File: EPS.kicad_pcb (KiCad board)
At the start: 4 copper layers, 90.2 x 95.9 mm, 197 parts, among them IC1 BQ7791514PWR, IC10 INA260AIPWR, IC12 LM74700QDBVRQ1, IC13 LM74700QDBVRQ1, IC14 LM5176PWPR, IC15 SN65HVD1782QDRQ1, IC16 TPS2121RUXR, IC17 TCAN1046AVDRQ1, IC18 INA260AIPWR, IC19 LM5060Q1MM_NOPB, IC2 INA260AIPWR, IC20 LM5060Q1MM_NOPB, IC21 MCP2517FD-H_SL, IC3 INA260AIPWR, IC4 INA260AIPWR, IC5 TPS22990DMLR, IC6 TPS22990DMLR, IC7 TPS22990DMLR, IC9 INA260AIPWR, J1 Barrel_Jack_Switch, J2 PH1RA-02-UA, J3 WJ126V-5.0-2P, J4 USB_C_Receptacle_USB2.0_16P, J6 TagConnect_TC2030-NL, Q10 BSZ067N06LS3_G, Q11 BSZ067N06LS3_G, Q12 BSZ067N06LS3_G, Q13 BSZ067N06LS3_G, Q15 BSZ067N06LS3_G, Q16 BSZ067N06LS3_G, Q5 BSZ067N06LS3_G, Q6 BSZ067N06LS3_G, Q8 BSZ067N06LS3_G, Q9 BSZ067N06LS3_G, U2 RP2354A_60QFN, Y1 ABM8AIG-20MHz-12-2Z-T3, Y2 ABM8-272-T3

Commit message: Rev 1 version
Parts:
- removed C36, C41, C43, C44, C46, C47, C50, C54, C57, C58, C59, C60, C61, C62, C63, C64, C66, C67, C75, C89, C90, C91, C92: 100n, Capacitor_SMD:C_0402_1005Metric
- removed C37, C42, C45, C48: 22u, Capacitor_SMD:C_0603_1608Metric
- removed C40: 22n, Capacitor_SMD:C_0402_1005Metric
- removed C49, C51, C55, C73, C74: 1u, Capacitor_SMD:C_0603_1608Metric
- removed C52, C53, C56: 220p, Capacitor_SMD:C_0402_1005Metric
- removed C65, C70, C71, C72: 4u7, Capacitor_SMD:C_0603_1608Metric
- removed C68, C69, C93, C94: 15p, Capacitor_SMD:C_0402_1005Metric
- removed D10, D11, D12, D13: SMCJ36A, HEDGE2:SMCJ36A
- removed D14, D5, D6, D7: CDBA240LL-HF, 40V 2A, HEDGE2:CDBA240LL-HF
- removed IC13: LM74700QDBVRQ1, HEDGE2:LM74700QDBVRQ1
- removed IC14: LM5176PWPR, HEDGE2:LM5176PWPR
- removed IC15: SN65HVD1782QDRQ1, HEDGE2:SN65HVD1782QDRQ1
- removed IC16: TPS2121RUXR, HEDGE2:TPS2121RUXR
- removed IC17: TCAN1046AVDRQ1, HEDGE2:TCAN1046AVDRQ1
- removed IC18, IC4: INA260AIPWR, HEDGE2:INA260AIPWR
- removed IC19, IC20: LM5060Q1MM_NOPB, HEDGE2:LM5060Q1MM_NOPB
- removed IC21: MCP2517FD-H_SL, HEDGE2:MCP2517FD-H_SL
- removed IC5, IC6: TPS22990DMLR, HEDGE2:TPS22990DMLR
- removed J3: WJ126V-5.0-2P, HEDGE2:WJ126V-5.0-2P
- removed J4: USB_C_Receptacle_USB2.0_16P, Connector_USB:USB_C_Receptacle_HCTL_HC-TYPE-C-16P-01A
- removed J6: TagConnect_TC2030-NL, Connector:Tag-Connect_TC2030-IDC-NL_2x03_P1.27mm_Vertical
- removed L3: 0630CDMCDDS-1R2MC, HEDGE2:0630CDMCDDS-1R2MC
- removed PS1: TLV75733PDBVR, HEDGE2:TLV75733PDBVR
- removed Q10, Q11, Q12, Q13, Q15, Q16, Q5, Q6, Q8, Q9: BSZ067N06LS3_G, HEDGE2:BSZ067N06LS3G
- removed R13: 450k, Resistor_SMD:R_0402_1005Metric
- removed R14, R30, R38: 100k, Resistor_SMD:R_0402_1005Metric
- removed R15, R39, R41, R43, R53, TH1: 10k, Resistor_SMD:R_0402_1005Metric
- removed R24, R25: 100, Resistor_SMD:R_0402_1005Metric
- removed R26: 93k1, Resistor_SMD:R_0402_1005Metric
- removed R27: 23k2, Resistor_SMD:R_0402_1005Metric
- removed R28: 7k5, Resistor_SMD:R_0402_1005Metric
- removed R29, R37: 9k09, Resistor_SMD:R_0402_1005Metric
- removed R31, R34: 200k, Resistor_SMD:R_0402_1005Metric
- removed R32, R35: 38k3, Resistor_SMD:R_0402_1005Metric
- removed R33, R36: 14k, Resistor_SMD:R_0402_1005Metric
- removed R40, R42: 27, Resistor_SMD:R_0402_1005Metric
- removed R44: 1k, Resistor_SMD:R_0402_1005Metric
- removed R45: 33, Resistor_SMD:R_0402_1005Metric
- removed R46, R48: 23k7, Resistor_SMD:R_0402_1005Metric
- removed R47, R49: 5k, Resistor_SMD:R_0402_1005Metric
- removed R50: 51k1, Resistor_SMD:R_0402_1005Metric
- removed R51, R52, R72: 4k7, Resistor_SMD:R_0402_1005Metric
- removed R54, R69: 60, Resistor_SMD:R_0402_1005Metric
- removed R70, R71: 5k1, Resistor_SMD:R_0402_1005Metric
- added A1: RaspberryPi_Pico, Module:RaspberryPi_Pico_SMD_HandSolder, F.Cu at (154.8, 119.7)
- added BT2: 1043, HEDGE2-EPS:BAT_1043, B.Cu at (152.8, 103.0)
- added BT3: 1043, HEDGE2-EPS:BAT_1043, B.Cu at (152.8, 80.8)
- added D9: SM712-02HTG, HEDGE2-EPS:SM71202HTG, F.Cu at (175.2, 97.2)
- added IC11: MCP2518FDT-E_SL, HEDGE2-EPS:MCP2518FDT-E_SL, F.Cu at (119.6, 113.7)
- added IC8: TPS22997RYZR, HEDGE2-EPS:TPS22997RYZR, F.Cu at (175.6, 71.5)
- added Q1: SI4497DY-T1-GE3, HEDGE2-EPS:SI4497DY-T1-GE3, B.Cu at (192.5, 66.0)
- added U1: INA260, Package_SO:TSSOP-16_4.4x5mm_P0.65mm, F.Cu at (167.7, 82.9)
- added U3: INA260, Package_SO:TSSOP-16_4.4x5mm_P0.65mm, F.Cu at (145.9, 73.9)
- added U4: INA260, Package_SO:TSSOP-16_4.4x5mm_P0.65mm, F.Cu at (170.0, 89.9)
- added U5: INA260, Package_SO:TSSOP-16_4.4x5mm_P0.65mm, F.Cu at (187.7, 89.5)
- BT1: value BK-18650-PC6 -> 1043; footprint HEDGE2:BK18650PC6 -> HEDGE2-EPS:BAT_1043
- C1, C12, C13, C14, C25, C26, C28, C8, C9: footprint Capacitor_SMD:C_0402_1005Metric -> Capacitor_SMD:C_0603_1608Metric
- C10, C11: value 100n -> 22u; footprint Capacitor_SMD:C_0402_1005Metric -> Capacitor_SMD:C_1206_3216Metric
- C15, C17: value 33u -> 100n
- C16: value 33u -> 1n
- C18: value 10u -> 1n
- C19: value 10u -> 100n
- C2, C3: value 1u -> 47u; footprint Capacitor_SMD:C_0603_1608Metric -> Capacitor_SMD:C_1206_3216Metric; moved to F.Cu
- C20, C22: value 22u -> 1n
- C21: value 22u -> 100n
- C23, C24: value 220u -> 100n
- C27: value 1u -> 100n
- C29: value 47p -> 100n; footprint Capacitor_SMD:C_0402_1005Metric -> Capacitor_SMD:C_0603_1608Metric
- C30, C31: value 15n -> 10p; footprint Capacitor_SMD:C_0402_1005Metric -> Capacitor_SMD:C_0603_1608Metric
- C32: value 22n -> 10p; footprint Capacitor_SMD:C_0402_1005Metric -> Capacitor_SMD:C_0603_1608Metric
- C33: value 180p -> 10p; footprint Capacitor_SMD:C_0402_1005Metric -> Capacitor_SMD:C_0603_1608Metric
- C34: value 100p -> 100n; footprint Capacitor_SMD:C_0402_1005Metric -> Capacitor_SMD:C_0603_1608Metric
- C35: value 47u -> 10uF
- C4, C5: value 100n -> 47u; footprint Capacitor_SMD:C_0402_1005Metric -> Capacitor_SMD:C_1206_3216Metric; moved to F.Cu
- C6, C7: footprint Capacitor_SMD:C_0402_1005Metric -> Capacitor_SMD:C_0603_1608Metric; moved to F.Cu
- D1: value SMCJ36A -> Zener; footprint HEDGE2:SMCJ36A -> Diode_SMD:D_SOD-123
- D2: value CDBA240LL-HF, 40V 2A -> Schottky; footprint HEDGE2:CDBA240LL-HF -> Diode_SMD:D_SOD-123; moved to F.Cu
- D3: value CDBA240LL-HF, 40V 2A -> LED; footprint HEDGE2:CDBA240LL-HF -> LED_SMD:LED_0603_1608Metric; moved to F.Cu
- D4: value CDBA240LL-HF, 40V 2A -> LED; footprint HEDGE2:CDBA240LL-HF -> LED_SMD:LED_0603_1608Metric
- H1EPS1, H2EPS1: footprint HEDGE2:SAMTEC_ESQ-126-39-G-D -> HEDGE2-EPS:SAMTEC_ESQ-126-39-G-D
- IC1: value BQ7791514PWR -> TPS22997RYZR; footprint HEDGE2:BQ7791501PWR -> HEDGE2-EPS:TPS22997RYZR; moved to F.Cu
- IC10: value INA260AIPWR -> SN65HVD1782QDRQ1; footprint HEDGE2:INA260AIPWR -> HEDGE2-EPS:SN65HVD1782QDRQ1
- IC12: value LM74700QDBVRQ1 -> MCP2518FDT-E_SL; footprint HEDGE2:LM74700QDBVRQ1 -> HEDGE2-EPS:MCP2518FDT-E_SL
- IC2: value INA260AIPWR -> TPS56C230RJER; footprint HEDGE2:INA260AIPWR -> HEDGE2-EPS:TPS56C230RJER
- IC3: value INA260AIPWR -> TPS22997RYZR; footprint HEDGE2:INA260AIPWR -> HEDGE2-EPS:TPS22997RYZR
- IC7: value TPS22990DMLR -> TPS22997RYZR; footprint HEDGE2:TPS22990DMLR -> HEDGE2-EPS:TPS22997RYZR
- IC9: value INA260AIPWR -> TCAN1046AVDYYRQ1; footprint HEDGE2:INA260AIPWR -> HEDGE2-EPS:TCAN1046AVDYYRQ1
- J1: value Barrel_Jack_Switch -> S4B-XH-A_LF__SN_; footprint Connector_BarrelJack:BarrelJack_CUI_PJ-102AH_Horizontal -> HEDGE2-EPS:S4BXHALFSN
- J2: footprint HEDGE2:PH1RA02UA -> HEDGE2-EPS:PH1RA02UA
- L1: value 3u3 AOTA-B201610S3R3-101-T -> 3u3; footprint HEDGE2:AOTAB201610S3R3101T -> HEDGE2-EPS:744393465033
- R1: value 1k -> 100k; footprint Resistor_SMD:R_0402_1005Metric -> Resistor_SMD:R_0603_1608Metric; moved to F.Cu
- R10, R11, R9: value 1M -> 4k7; footprint Resistor_SMD:R_0402_1005Metric -> Resistor_SMD:R_0603_1608Metric; moved to F.Cu
- R12: value 3M3 -> 2k2; footprint Resistor_SMD:R_0402_1005Metric -> Resistor_SMD:R_0603_1608Metric; moved to F.Cu
- R16: value 10k -> 60; footprint Resistor_SMD:R_0402_1005Metric -> Resistor_SMD:R_0603_1608Metric; moved to F.Cu
- R17: value 10 -> 60; footprint Resistor_SMD:R_0402_1005Metric -> Resistor_SMD:R_0603_1608Metric
- R18: value 249k -> 60; footprint Resistor_SMD:R_0402_1005Metric -> Resistor_SMD:R_0603_1608Metric
- R19: value 71k5 -> 60; footprint Resistor_SMD:R_0402_1005Metric -> Resistor_SMD:R_0603_1608Metric
- R2: value 9m -> 110k; footprint Resistor_SMD:R_0402_1005Metric -> Resistor_SMD:R_0603_1608Metric
- R20: value 2k -> 10k; footprint Resistor_SMD:R_0402_1005Metric -> Resistor_SMD:R_0603_1608Metric
- R21: value 105k -> 10k; footprint Resistor_SMD:R_0402_1005Metric -> Resistor_SMD:R_0603_1608Metric
- R22: value 20k -> 10; footprint Resistor_SMD:R_0402_1005Metric -> Resistor_SMD:R_0603_1608Metric
- R23: value 10k -> 10; footprint Resistor_SMD:R_0402_1005Metric -> Resistor_SMD:R_0603_1608Metric
- R3: value 1k -> 15k; footprint Resistor_SMD:R_0402_1005Metric -> Resistor_SMD:R_0603_1608Metric; moved to F.Cu
- R4: value 1k -> 180k; footprint Resistor_SMD:R_0402_1005Metric -> Resistor_SMD:R_0603_1608Metric; moved to F.Cu
- R5: value 1k -> 33k; footprint Resistor_SMD:R_0402_1005Metric -> Resistor_SMD:R_0603_1608Metric; moved to F.Cu
- R6: value 1k -> 205k; footprint Resistor_SMD:R_0402_1005Metric -> Resistor_SMD:R_0603_1608Metric; moved to F.Cu
- R7: value 10m -> 51k1; footprint Resistor_SMD:R_0402_1005Metric -> Resistor_SMD:R_0603_1608Metric; moved to F.Cu
- R8: value 4k5 -> 10k; footprint Resistor_SMD:R_0402_1005Metric -> Resistor_SMD:R_0603_1608Metric
- U2: value RP2354A_60QFN -> INA260; footprint HEDGE2:RP2354A -> Package_SO:TSSOP-16_4.4x5mm_P0.65mm
- Y1: value ABM8AIG-20MHz-12-2Z-T3 -> 40MHz; footprint Crystal:Crystal_SMD_3225-4Pin_3.2x2.5mm -> HEDGE2-EPS:ABM10AIG-40.000MHZ-7-J1Z-T
- Y2: value ABM8-272-T3 -> 40MHz; footprint Crystal:Crystal_SMD_3225-4Pin_3.2x2.5mm -> HEDGE2-EPS:ABM10AIG-40.000MHZ-7-J1Z-T
- moved D4 155.2 mm to (112.2, 71.5)
- moved R11 148.5 mm to (112.2, 73.4), turned to 0 degrees
- moved J2 144.1 mm to (118.0, 67.7), turned to 90 degrees
- moved R12 142.9 mm to (112.0, 79.2)
- moved H2EPS1 138.0 mm to (122.7, 60.4)
- moved C27 137.9 mm to (124.0, 91.5), turned to 0 degrees
- moved C26 137.1 mm to (118.2, 85.7), turned to 90 degrees
- moved IC9 136.8 mm to (119.9, 93.3), turned to 90 degrees
- moved H1EPS1 135.1 mm to (122.7, 65.5)
- moved C7 134.5 mm to (134.3, 78.7), turned to 180 degrees
- moved D3 134.4 mm to (112.0, 77.5)
- moved C28 133.6 mm to (121.4, 85.7), turned to 90 degrees
- moved C35 133.2 mm to (119.2, 98.7), turned to 180 degrees
- moved R6 131.6 mm to (132.4, 86.5), turned to 0 degrees
- moved R16 130.4 mm to (117.4, 88.9)
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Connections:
- net /UART_E_RX renamed /UART_E_RX (SCI)
- net /UART_E_TX renamed /UART_E_TX (SCI)
- net /UART_F_RX renamed /UART_F_RX (GNSS_RXD1)
- net /UART_F_TX renamed /UART_F_TX (GNSS_TXD1)
- C1 pad 1: 3V3 -> Net-(IC2-BST)
- C1 pad 2: GND -> Net-(IC2-SW_1)
- C10 pad 1: +3V3 -> +BATT_SENSE
- C11 pad 1: +3V3 -> +BATT_SENSE
- C14 pad 1: Net-(IC14-VIN) -> +3V3
- C15 pad 1: +BUCK_BOOST -> +5V_OBC_SENSE
- C16 pad 1: +BUCK_BOOST -> Net-(IC1-CT)
- C17 pad 1: +BUCK_BOOST -> +5V_SCI_SENSE
- C18 pad 1: +BUCK_BOOST -> Net-(IC3-CT)
- C19 pad 1: +BUCK_BOOST -> +5V_COMM_SENSE
- C2 pad 1: Net-(IC1-VDD) -> +5V
- C20 pad 1: +5V_BUCK_BOOST -> Net-(IC7-CT)
- C21 pad 1: +5V_BUCK_BOOST -> +5V_GNSS_SENSE
- C22 pad 1: +5V_BUCK_BOOST -> Net-(IC8-CT)
- C23 pad 1: +5V_BUCK_BOOST -> +3V3
- C24 pad 1: +5V_BUCK_BOOST -> +3V3
- C25 pad 1: /Power Conversion/BIAS -> +5V
- C26 pad 1: Net-(D4-K) -> Net-(C26-Pad1)
- C26 pad 2: /Power Conversion/SW2 -> GND
- C27 pad 1: /Power Conversion/VCC -> +3V3
- C28 pad 1: /Power Conversion/SW1 -> Net-(C28-Pad1)
- C28 pad 2: Net-(D7-K) -> GND
- C29 pad 1: Net-(IC14-CSG) -> +3V3
- C29 pad 2: Net-(IC14-CS) -> GND
- C3 pad 1: GND -> +5V
- C3 pad 2: Net-(IC1-AVDD) -> GND
- C30 pad 1: Net-(IC14-SS) -> Net-(IC11-OSC1)
- C31 pad 1: Net-(IC14-COMP) -> Net-(IC11-OSC2)
- C31 pad 2: Net-(C31-Pad2) -> GND
- C32 pad 1: -BATT_IN -> Net-(IC12-OSC2)
- C33 pad 1: Net-(IC14-COMP) -> Net-(IC12-OSC1)
- C34 pad 1: Net-(IC14-SLOPE) -> +3V3
- C35 pad 1: +BUCK_BOOST -> +5V
- C4 pad 1: Net-(IC1-VC3) -> +5V
- C4 pad 2: Net-(IC1-VC2) -> GND
- C5 pad 1: Net-(IC1-VC2) -> +5V
- C5 pad 2: Net-(IC1-VC1) -> GND
- C6 pad 1: Net-(IC1-VC1) -> Net-(IC2-VCC)
- C7 pad 1: GND -> +BATT_SENSE
- C7 pad 2: Net-(IC1-VC0) -> GND
- D1 pad 1: +BATT -> /EN
- D2 pad 1: Net-(D2-K) -> Net-(A1-VSYS)
- D2 pad 2: Net-(D2-A) -> +5V
- D3 pad 2: PACK- -> +5V
- D4 pad 2: /Power Conversion/VCC -> +BATT_SENSE
- H1EPS1 pad 05: /UART_A_TX -> unconnected-(H1EPS1-Pad05)
- H1EPS1 pad 06: /UART_B_TX -> unconnected-(H1EPS1-Pad06)
- H1EPS1 pad 07: /UART_A_RX -> unconnected-(H1EPS1-Pad07)
- H1EPS1 pad 08: /UART_B_RX -> unconnected-(H1EPS1-Pad08)
- H1EPS1 pad 13: /UART_C_TX -> unconnected-(H1EPS1-Pad13)
- H1EPS1 pad 15: /UART_C_RX -> unconnected-(H1EPS1-Pad15)
- H1EPS1 pad 22: /UART_D_TX -> unconnected-(H1EPS1-Pad22)
- H1EPS1 pad 24: /UART_D_RX -> unconnected-(H1EPS1-Pad24)
- H1EPS1 pad 25: /5V_PERM -> unconnected-(H1EPS1-Pad25)
- H1EPS1 pad 26: /5V_PERM -> unconnected-(H1EPS1-Pad26)
- H1EPS1 pad 29: GND -> unconnected-(H1EPS1-Pad29)
- H1EPS1 pad 30: GND -> unconnected-(H1EPS1-Pad30)
- H1EPS1 pad 31: GND -> unconnected-(H1EPS1-Pad31)
- H1EPS1 pad 32: GND -> unconnected-(H1EPS1-Pad32)
- H1EPS1 pad 33: unconnected-(H1EPS1-Pad33) -> GND
- H1EPS1 pad 34: unconnected-(H1EPS1-Pad34) -> GND
- H1EPS1 pad 41: unconnected-(H1EPS1-Pad41) -> /UART_G_TX (EPS)
- H1EPS1 pad 43: unconnected-(H1EPS1-Pad43) -> /UART_G_RX (EPS)
- H1EPS1 pad 45: /ENA_PWR_1 -> unconnected-(H1EPS1-Pad45)
- H1EPS1 pad 46: /PWR_1 -> +5V_OBC
- H1EPS1 pad 47: /ENA_PWR_2 -> unconnected-(H1EPS1-Pad47)
- H1EPS1 pad 48: /PWR_2 -> +5V_GNSS
- H1EPS1 pad 49: /ENA_PWR_3 -> unconnected-(H1EPS1-Pad49)
- H1EPS1 pad 50: /PWR_3 -> +5V_SCI
- H1EPS1 pad 51: /ENA_PWR_4 -> unconnected-(H1EPS1-Pad51)
- H1EPS1 pad 52: /PWR_4 -> +5V_COMM
- H2EPS1 pad 01: unconnected-(H2EPS1-Pad01) -> /DIN/CONFIG/DIO14_XB
- H2EPS1 pad 02: unconnected-(H2EPS1-Pad02) -> /DOUT/DIO13_XB
- H2EPS1 pad 03: unconnected-(H2EPS1-Pad03) -> /RTS/DIO6_XB
- H2EPS1 pad 04: unconnected-(H2EPS1-Pad04) -> /CTS/DIO7_XB
- H2EPS1 pad 05: unconnected-(H2EPS1-Pad05) -> /AD3/DIO3/SPI_SSEL_XB
- H2EPS1 pad 06: unconnected-(H2EPS1-Pad06) -> /AD/DIO2/SPI_CLK_XB
- H2EPS1 pad 07: unconnected-(H2EPS1-Pad07) -> /DIO4/SPI_MOSI_XB
- H2EPS1 pad 08: unconnected-(H2EPS1-Pad08) -> /DIO12/SPI_MISO_XB
- H2EPS1 pad 09: unconnected-(H2EPS1-Pad09) -> /DTR/SLEEP_RQ/DIO8_XB
- H2EPS1 pad 10: unconnected-(H2EPS1-Pad10) -> /AD1/DIO1/SPI_ATTN_XB
- H2EPS1 pad 11: unconnected-(H2EPS1-Pad11) -> /ON_SLEEP/DIO9_XB
- H2EPS1 pad 12: unconnected-(H2EPS1-Pad12) -> /DIO10/PWM0_XB
- H2EPS1 pad 13: unconnected-(H2EPS1-Pad13) -> /RESET_XB
- H2EPS1 pad 14: unconnected-(H2EPS1-Pad14) -> /DIO11/PWM1_XB
- H2EPS1 pad 15: unconnected-(H2EPS1-Pad15) -> /AD0/DIO0_XB
- H2EPS1 pad 16: unconnected-(H2EPS1-Pad16) -> /Associate/DIO5_XB
- H2EPS1 pad 17: unconnected-(H2EPS1-Pad17) -> /NDTR_XB
- H2EPS1 pad 19: unconnected-(H2EPS1-Pad19) -> /MIC_IN_DMR
- H2EPS1 pad 20: unconnected-(H2EPS1-Pad20) -> /LINE_OUT_DMR
- H2EPS1 pad 21: unconnected-(H2EPS1-Pad21) -> /T/R_DMR
- H2EPS1 pad 22: unconnected-(H2EPS1-Pad22) -> /PTT_DMR
- H2EPS1 pad 23: unconnected-(H2EPS1-Pad23) -> /SPKEN_DMR
- H2EPS1 pad 24: unconnected-(H2EPS1-Pad24) -> /CS_DMR
- H2EPS1 pad 25: /5V_PERM -> /HST_RXD_DMR
- H2EPS1 pad 26: /5V_PERM -> /UART_RX_DMR
- H2EPS1 pad 27: unconnected-(H2EPS1-Pad27) -> /HST_TXD_DMR
- H2EPS1 pad 28: unconnected-(H2EPS1-Pad28) -> /UART_TX_DMR
- H2EPS1 pad 33: /ENA_PWR_5 -> unconnected-(H2EPS1-Pad33)
- H2EPS1 pad 34: /PWR_5 -> unconnected-(H2EPS1-Pad34)
- H2EPS1 pad 35: /ENA_PWR_6 -> unconnected-(H2EPS1-Pad35)
- H2EPS1 pad 36: /PWR_6 -> unconnected-(H2EPS1-Pad36)
- H2EPS1 pad 37: /ENA_PWR_7 -> unconnected-(H2EPS1-Pad37)
- H2EPS1 pad 38: /PWR_7 -> unconnected-(H2EPS1-Pad38)
- H2EPS1 pad 39: /ENA_PWR_8 -> unconnected-(H2EPS1-Pad39)
- H2EPS1 pad 40: /PWR_8 -> unconnected-(H2EPS1-Pad40)
- H2EPS1 pad 41: unconnected-(H2EPS1-Pad41) -> BATT
- H2EPS1 pad 42: unconnected-(H2EPS1-Pad42) -> BATT
- H2EPS1 pad 43: /CHARGE -> BATT
- H2EPS1 pad 44: /CHARGE -> BATT
- H2EPS1 pad 45: /BATT -> BATT
- H2EPS1 pad 46: /BATT -> BATT
- H2EPS1 pad 47: /RBF_A -> unconnected-(H2EPS1-Pad47)
- H2EPS1 pad 48: /DS_A -> unconnected-(H2EPS1-Pad48)
- H2EPS1 pad 49: /RBF_B -> unconnected-(H2EPS1-Pad49)
- H2EPS1 pad 50: /DS_B -> unconnected-(H2EPS1-Pad50)
- H2EPS1 pad 51: /RBF_C -> unconnected-(H2EPS1-Pad51)
- H2EPS1 pad 52: /DS_C -> unconnected-(H2EPS1-Pad52)
- IC1 pad 1: Net-(IC1-VDD) -> +5V_OBC_SENSE
- IC1 pad 10: GND -> /OBC_C
- IC1 pad 2: Net-(IC1-AVDD) -> +5V_OBC_SENSE
- IC1 pad 3: Net-(IC1-VC3) -> +5V_OBC_SENSE
- IC1 pad 4: Net-(IC1-VC3) -> unconnected-(IC1-PG-Pad4)
- IC1 pad 5: Net-(IC1-VC3) -> GND
- IC1 pad 6: Net-(IC1-VC2) -> +5V_OBC
- IC1 pad 7: Net-(IC1-VC1) -> +5V_OBC
- IC1 pad 8: Net-(IC1-VC0) -> +5V_OBC
- IC1 pad 9: GND -> Net-(IC1-CT)
- IC10 pad 1: +EPS_5V -> /RS485_RX
- IC10 pad 2: +EPS_5V -> /RS485_E
- IC10 pad 3: +EPS_5V -> /RS485_E
- IC10 pad 4: +3V3 -> /RS485_TX
- IC10 pad 5: SDA -> GND
- IC10 pad 6: GND -> Net-(IC10-A)
- IC10 pad 7: unconnected-(IC10-ALERT-Pad7) -> Net-(IC10-B)
- IC10 pad 8: SDA -> +3V3
- IC12 pad 1: Net-(IC12-VCAP) -> /TXCAN_B
- IC12 pad 2: GND -> /RXCAN_B
- IC12 pad 3: -BATT_IN -> unconnected-(IC12-CLKO/SOF-Pad3)
- IC12 pad 4: +BUCK_BOOST -> /CAN_B_INT
- IC12 pad 5: Net-(IC12-GATE) -> Net-(IC12-OSC2)
- IC12 pad 6: -BATT_IN -> Net-(IC12-OSC1)
- IC2 pad 1: +5V_OBC_IN -> Net-(IC2-BST)
- IC2 pad 10: +3V3 -> GND
- IC2 pad 11: GND -> unconnected-(IC2-SS-Pad11)
- IC2 pad 12: +5V_OBC_IN -> /EN
- IC2 pad 13: unconnected-(IC2-NC-Pad13) -> GND
- IC2 pad 14: -5V_OBC_IN -> Net-(IC2-FB)
- IC2 pad 15: -5V_OBC_IN -> Net-(IC2-MODE)
- IC2 pad 16: -5V_OBC_IN -> GND
- IC2 pad 2: +5V_OBC_IN -> +BATT_SENSE
- IC2 pad 3: +5V_OBC_IN -> +BATT_SENSE
- IC2 pad 4: GND -> +BATT_SENSE
- IC2 pad 5: SCL -> +BATT_SENSE
- IC2 pad 6: GND -> Net-(IC2-SW_1)
- IC2 pad 7: unconnected-(IC2-ALERT-Pad7) -> GND
- IC2 pad 8: SDA -> GND
- IC2 pad 9: SCL -> Net-(IC2-PGOOD)
- IC3 pad 1: +COMMS_IN -> +5V_SCI_SENSE
- IC3 pad 10: +3V3 -> /SCI_C
- IC3 pad 2: +COMMS_IN -> +5V_SCI_SENSE
- IC3 pad 3: +COMMS_IN -> +5V_SCI_SENSE
- IC3 pad 4: +3V3 -> unconnected-(IC3-PG-Pad4)
- IC3 pad 6: GND -> +5V_SCI
- IC3 pad 7: unconnected-(IC3-ALERT-Pad7) -> +5V_SCI
- IC3 pad 8: SDA -> +5V_SCI
- IC3 pad 9: SCL -> Net-(IC3-CT)
- IC7 pad 1: Net-(IC7-CT) -> +5V_COMM_SENSE
- IC7 pad 10: +SCI_IN -> /COMM_C
- IC7 pad 2: unconnected-(IC7-NC-Pad2) -> +5V_COMM_SENSE
- IC7 pad 3: +5V_BUCK_BOOST -> +5V_COMM_SENSE
- IC7 pad 4: +5V_BUCK_BOOST -> unconnected-(IC7-PG-Pad4)
- IC7 pad 5: SCI_EN -> GND
- IC7 pad 6: GND -> +5V_COMM
- IC7 pad 7: Net-(IC7-PG) -> +5V_COMM
- IC7 pad 8: +SCI_IN -> +5V_COMM
- IC7 pad 9: +SCI_IN -> Net-(IC7-CT)
- IC9 pad 1: +BENCH_IN -> /TXCAN_A
- IC9 pad 10: +3V3 -> /CAN_B_H
- IC9 pad 11: GND -> +3V3
- IC9 pad 12: +BENCH_IN -> /CAN_A_L
- IC9 pad 13: unconnected-(IC9-NC-Pad13) -> /CAN_A_H
- IC9 pad 14: -BENCH_IN -> GND
- IC9 pad 2: +BENCH_IN -> GND
- IC9 pad 3: +BENCH_IN -> +5V
- IC9 pad 4: GND -> /RXCAN_A
- IC9 pad 5: SDA -> GND
- IC9 pad 6: GND -> /TXCAN_B
- IC9 pad 7: unconnected-(IC9-ALERT-Pad7) -> /RXCAN_B
- IC9 pad 8: SDA -> GND
- IC9 pad 9: SCL -> /CAN_B_L
- J1 pad 1: +BATT -> GND
- J1 pad 2: PACK- -> /VC1
- J1 pad 3: unconnected-(J1-Pad3) -> /VC2
- J2 pad 1: /RBF_INHIBIT -> /EN
- L1 pad 1: 1V1 -> Net-(IC2-SW_1)
- L1 pad 2: Net-(U2-VREG_LX) -> +5V
- R1 pad 1: +BATT -> Net-(IC2-PGOOD)
- R1 pad 2: Net-(IC1-VDD) -> Net-(IC2-VCC)
- R10 pad 1: Net-(D2-A) -> +3V3
- R10 pad 2: Net-(IC1-CHG) -> /SDA
- R11 pad 1: Net-(D2-K) -> Net-(D4-K)
- R11 pad 2: Net-(D2-A) -> GND
- R12 pad 1: PACK- -> Net-(D3-K)
- R12 pad 2: Net-(D2-K) -> GND
- R16 pad 1: Net-(IC1-VTB) -> /CAN_A_H
- R16 pad 2: GND -> Net-(C26-Pad1)
- R17 pad 1: Net-(IC14-VIN) -> Net-(C26-Pad1)
- R17 pad 2: Net-(D6-K) -> /CAN_A_L
- R18 pad 1: Net-(IC14-EN/UVLO) -> /CAN_B_H
- R18 pad 2: +BUCK_BOOST -> Net-(C28-Pad1)
- R19 pad 1: GND -> Net-(C28-Pad1)
- R19 pad 2: Net-(IC14-EN/UVLO) -> /CAN_B_L
- R2 pad 1: /Power Conversion/RCS -> +5V
- R2 pad 2: GND -> Net-(IC2-FB)
- R20 pad 1: Net-(IC14-VISNS) -> +3V3
- R20 pad 2: +BUCK_BOOST -> /RS485_RX
- R21 pad 1: +5V_BUCK_BOOST -> /RS485_E
- R21 pad 2: /Power Conversion/FB -> GND
- R22 pad 1: /Power Conversion/FB -> Net-(IC10-B)
- R22 pad 2: GND -> /UART_G_TX (EPS)
- R23 pad 1: /Power Conversion/VCC -> Net-(IC10-A)
- R23 pad 2: Net-(IC14-PGOOD) -> /UART_G_RX (EPS)
- R3 pad 1: +BATT -> Net-(IC2-FB)
- R3 pad 2: Net-(IC1-VC3) -> GND
- R4 pad 1: /Batteries/VC2 -> Net-(IC2-VCC)
- R4 pad 2: Net-(IC1-VC2) -> Net-(IC2-MODE)
- R5 pad 1: /Batteries/VC1 -> Net-(IC2-MODE)
- R5 pad 2: Net-(IC1-VC1) -> GND
- R6 pad 1: GND -> +BATT_SENSE
- R6 pad 2: Net-(IC1-VC0) -> /EN
- R7 pad 1: GND -> /EN
- R7 pad 2: Net-(D5-A) -> GND
- R8 pad 1: Net-(Q8-G) -> GND
- R8 pad 2: Net-(IC1-DSG) -> Net-(Q1-G)
- R9 pad 1: Net-(D5-A) -> +3V3
- R9 pad 2: Net-(Q8-G) -> /SCL
- U2 pad 1: 3V3 -> +5V
- U2 pad 10: STATUS1 -> +3V3
- U2 pad 11: 3V3 -> GND
- U2 pad 12: STATUS2 -> +5V
- U2 pad 13: OBC_EN -> unconnected-(U2-NC-Pad13)
- U2 pad 14: COMM_EN -> +5V_SCI_SENSE
- U2 pad 15: SCI_EN -> +5V_SCI_SENSE
- U2 pad 16: unconnected-(U2-GPIO12-Pad16) -> +5V_SCI_SENSE
- U2 pad 2: unconnected-(U2-GPIO0-Pad2) -> +5V
- U2 pad 3: Net-(U2-GPIO1) -> +5V
- U2 pad 4: Net-(U2-GPIO2) -> GND
- U2 pad 5: unconnected-(U2-GPIO3-Pad5) -> /SCL
- U2 pad 6: 1V1 -> GND
- U2 pad 8: BOUNCEBATT -> /SDA
- U2 pad 9: BATTEN -> /SCL
- Y1 pad 1: Net-(C93-Pad2) -> Net-(IC11-OSC2)
- Y1 pad 3: Net-(IC21-OSC1) -> Net-(IC11-OSC1)
- Y2 pad 1: Net-(U2-XIN) -> Net-(IC12-OSC2)
- Y2 pad 3: Net-(C69-Pad2) -> Net-(IC12-OSC1)
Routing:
- net +3V3: track 0.00 -> 312.8 mm, vias 0 -> 7
- net /VC2: track 0.00 -> 203.1 mm
- net /SDA: track 0.00 -> 185.1 mm, vias 0 -> 11
- net /SCL: track 0.00 -> 185.1 mm, vias 0 -> 12
- net +5V: track 0.00 -> 160.0 mm, vias 0 -> 6
- net GND: track 0.00 -> 133.6 mm, vias 0 -> 73
- net /VC1: track 0.00 -> 108.3 mm
- net +BATT_NP: track 0.00 -> 97.9 mm
- net /SCK: track 0.00 -> 54.0 mm, vias 0 -> 2
- net /MISO: track 0.00 -> 53.6 mm, vias 0 -> 2
- net /OBC_C: track 0.00 -> 47.9 mm, vias 0 -> 6
- net /MOSI: track 0.00 -> 47.7 mm, vias 0 -> 4
- net /GNSS_C: track 0.00 -> 47.0 mm, vias 0 -> 6
- net /COMM_C: track 0.00 -> 42.9 mm, vias 0 -> 4
- net /SCI_C: track 0.00 -> 42.7 mm, vias 0 -> 4
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- added copper zone on F.Cu, net +5V
- added copper zone on F.Cu, net +5V_COMM
- added copper zone on F.Cu, net +5V_COMM_SENSE
- added copper zone on F.Cu, net +5V_GNSS
- added copper zone on F.Cu, net +5V_GNSS_SENSE
- added copper zone on F.Cu, net +5V_OBC
- added copper zone on F.Cu, net +5V_OBC_SENSE
- added copper zone on F.Cu, net +5V_SCI
- added copper zone on F.Cu, net +5V_SCI_SENSE
- added copper zone on B.Cu, net +BATT_NP
- added copper zone on F.Cu, net +BATT_SENSE
- added copper zone on B.Cu, net BATT
- added copper zone on F.Cu, net BATT
- added copper zone on F.Cu, net GND
- added copper zone on In1.Cu, net GND
- added copper zone on In2.Cu, net GND
- added copper zone on F.Cu, net Net-(IC2-BST)
- added copper zone on F.Cu, net Net-(IC2-SW_1)
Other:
- board text added: "${REFERENCE}"
- board text added: "+5V LED"
- board text added: "BATT LED"
- board text added: "HEDGE-2: EPS PCB Rev 1.0"
- board text removed: "EPS"

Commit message: Finished routing
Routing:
- net GND: track 133.6 -> 135.5 mm, vias 73 -> 145
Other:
- board text removed: "${REFERENCE}"

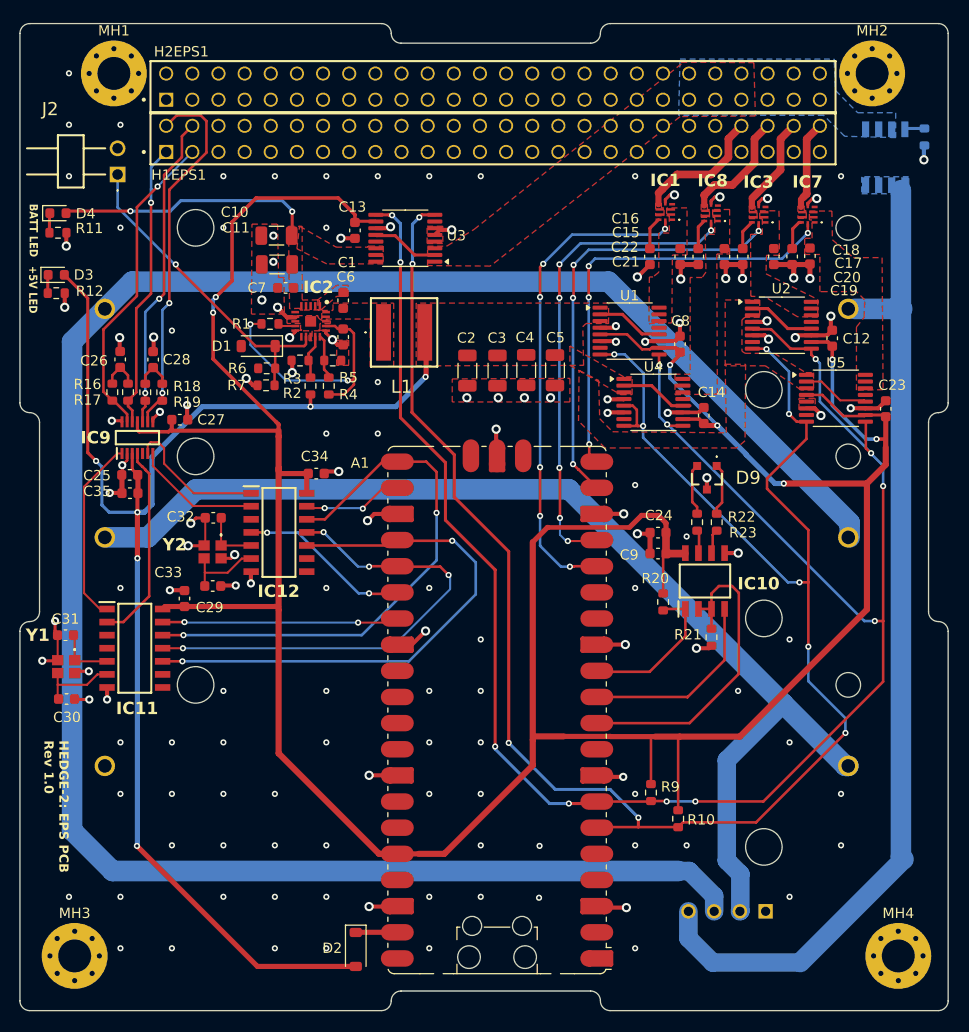
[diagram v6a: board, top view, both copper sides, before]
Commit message: Added sep switch connector and fixes
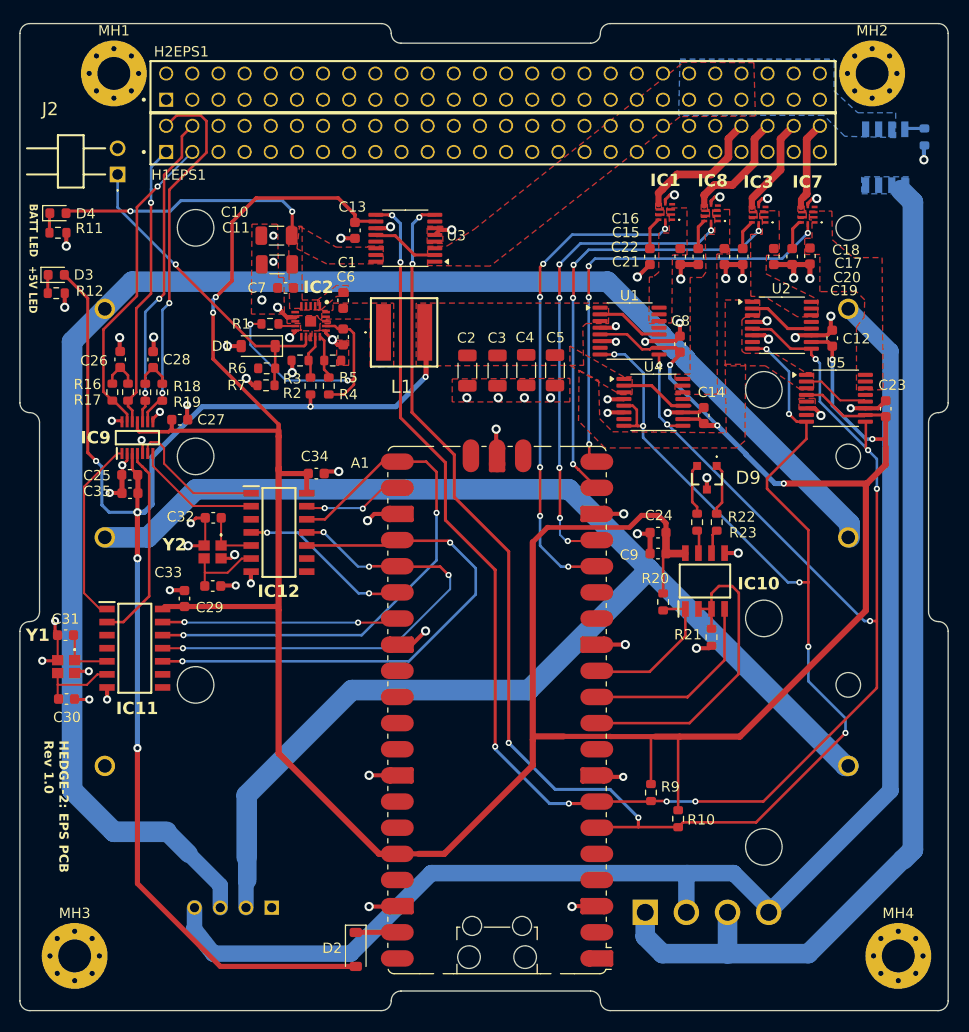
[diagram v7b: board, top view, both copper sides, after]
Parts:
- added J4: M80-5000000M1-04-333-00-000, HEDGE2-EPS:M805000000M10433300000, B.Cu at (169.2, 139.4)
- moved J1 48.0 mm to (132.9, 138.9)
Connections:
- BT3 pad P: +BATT_NP -> +BATT_BSW
- J1 pad 4: +BATT_NP -> +BATT_BSW
- Q1 pad 5: +BATT_NP -> +BATT_ASW
- Q1 pad 6: +BATT_NP -> +BATT_ASW
- Q1 pad 7: +BATT_NP -> +BATT_ASW
- Q1 pad 8: +BATT_NP -> +BATT_ASW
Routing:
- net +BATT_BSW: track 0.00 -> 133.2 mm
- net +BATT_ASW: track 0.00 -> 101.8 mm
- net +BATT_NP: track 97.9 -> 0.00 mm
- net /VC2: track 203.1 -> 153.1 mm
- net /VC1: track 108.3 -> 144.4 mm
- net GND: track 135.5 -> 137.7 mm, vias 145 -> 75
- net +5V: track 160.0 -> 162.0 mm
- net /SCL: track 185.2 -> 183.6 mm
- added copper zone on B.Cu, net +BATT_ASW
- removed copper zone on B.Cu, net +BATT_NP

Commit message: Fixed the rest of DRC errors
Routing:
- net /UART_G_RX (EPS): track 5.07 -> 45.4 mm, vias 0 -> 2
- net /UART_G_TX (EPS): track 5.03 -> 44.2 mm, vias 0 -> 2
- net /CAN_A_INT: track 0.00 -> 34.2 mm, vias 0 -> 2
- net +BATT_SENSE: track 25.7 -> 43.2 mm, vias 2 -> 5
- net Net-(IC2-SW_1): track 0.00 -> 7.26 mm, vias 0 -> 2
- net +3V3: track 312.5 -> 313.7 mm
- net GND: track 137.7 -> 137.1 mm
